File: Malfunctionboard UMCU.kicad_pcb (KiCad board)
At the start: 2 copper layers, 144.9 x 32.7 mm, 265 parts, among them J101 Conn_02x05_Odd_Even, J102 Conn_02x05_Odd_Even, J201 Conn_Coaxial, J202 Conn_Coaxial, J301 Conn_Coaxial, J302 Conn_Coaxial, J401 Conn_Coaxial, J402 Conn_Coaxial, J501 Conn_Coaxial, J502 Conn_Coaxial, J601 Conn_Coaxial, J602 Conn_Coaxial, J701 Conn_Coaxial, J702 Conn_Coaxial, J801 Conn_Coaxial, J802 Conn_Coaxial, J901 Conn_Coaxial, J902 Conn_Coaxial, Q101 NTR5103NT1G, Q102 RSC002P03T316, Q103 RSC002P03T316, Q104 NTR5103NT1G, Q201 NTR5103NT1G, Q202 NTR5103NT1G, Q301 NTR5103NT1G, Q302 NTR5103NT1G, Q401 NTR5103NT1G, Q402 NTR5103NT1G, Q501 NTR5103NT1G, Q502 NTR5103NT1G, Q601 NTR5103NT1G, Q602 NTR5103NT1G, Q701 NTR5103NT1G, Q702 NTR5103NT1G, Q801 NTR5103NT1G, Q802 NTR5103NT1G, Q901 NTR5103NT1G, Q902 NTR5103NT1G, U201 LM339PW, U301 LM339PW, U401 LM339PW, U501 LM339PW, U601 LM339PW, U701 LM339PW, U801 LM339PW, U901 LM339PW

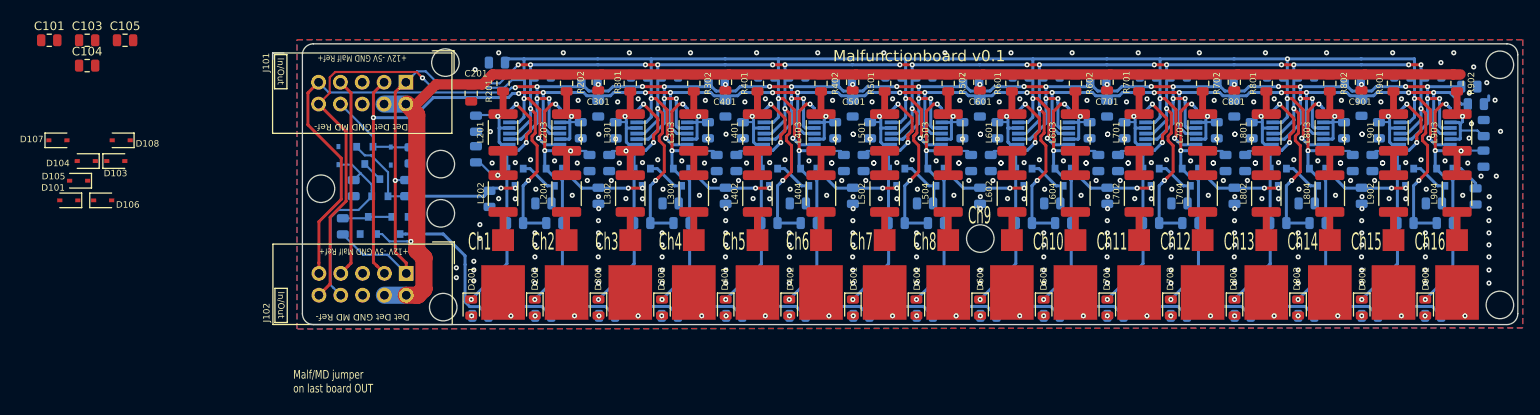
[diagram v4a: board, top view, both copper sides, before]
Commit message: changed: Added extra protection C's to v0.1
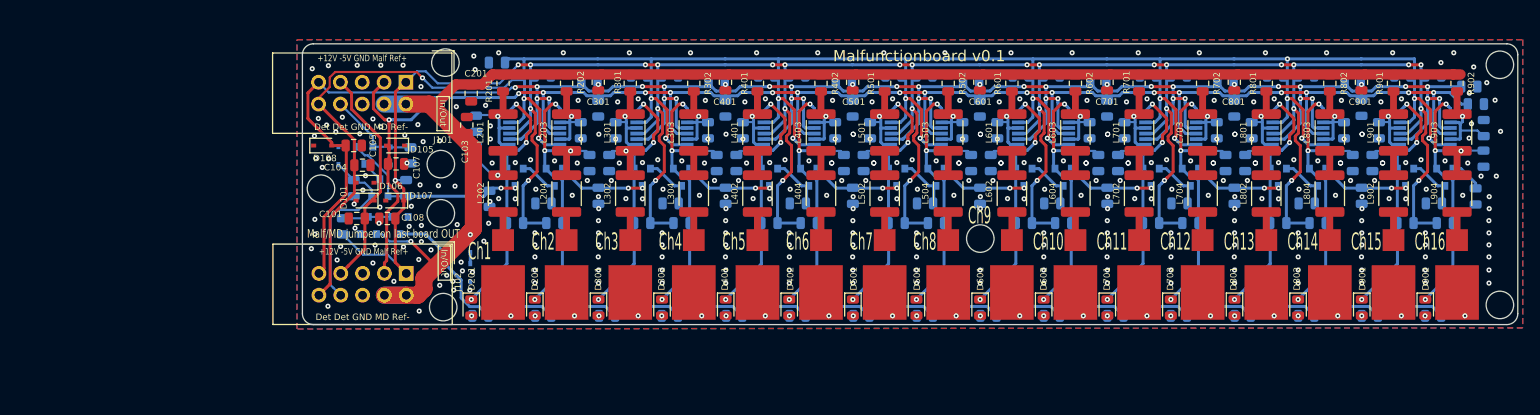
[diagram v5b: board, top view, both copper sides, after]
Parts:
- added C107: 10n, Capacitor_SMD:C_0805_2012Metric, F.Cu at (80.1, 114.9)
- added C108: 10n, Capacitor_SMD:C_0805_2012Metric, F.Cu at (79.1, 121.3)
- D103, D104: moved to B.Cu
- moved D104 46.5 mm to (88.7, 127.6), turned to 270 degrees
- moved C103 45.3 mm to (88.3, 110.4), turned to 270 degrees
- moved D103 42.4 mm to (88.7, 124.2), turned to 90 degrees
- moved C101 41.4 mm to (75.5, 121.3)
- moved D107 39.8 mm to (80.0, 119.2), turned to 180 degrees
- moved D105 37.1 mm to (80.1, 112.8)
- moved D101 34.5 mm to (76.5, 119.2)
- moved C104 34.1 mm to (76.2, 115.1), turned to 180 degrees
- moved D106 30.6 mm to (76.5, 117.1), turned to 180 degrees
- moved C105 29.3 mm to (75.2, 112.8), turned to 180 degrees
- moved D108 23.5 mm to (71.6, 112.8), turned to 0 degrees
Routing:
- net /V_in: track 157.7 -> 170.7 mm, vias 1 -> 2
- net /Malf: track 23.2 -> 26.5 mm
- net Net-(C106-Pad2): track 22.7 -> 21.2 mm
- net /Ref+: track 276.5 -> 277.8 mm
- net Net-(D103-Pad1): track 0.00 -> 1.29 mm
- net /sheet5DD8DCB3/LED_GND: track 142.3 -> 141.1 mm
- net /Ref-: track 301.0 -> 302.1 mm
- net -5V: track 209.5 -> 210.5 mm
- net +12V: track 374.8 -> 375.6 mm
- net GND: vias 301 -> 358
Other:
- board size 144.9 x 32.7 mm -> 141.4 x 32.7 mm

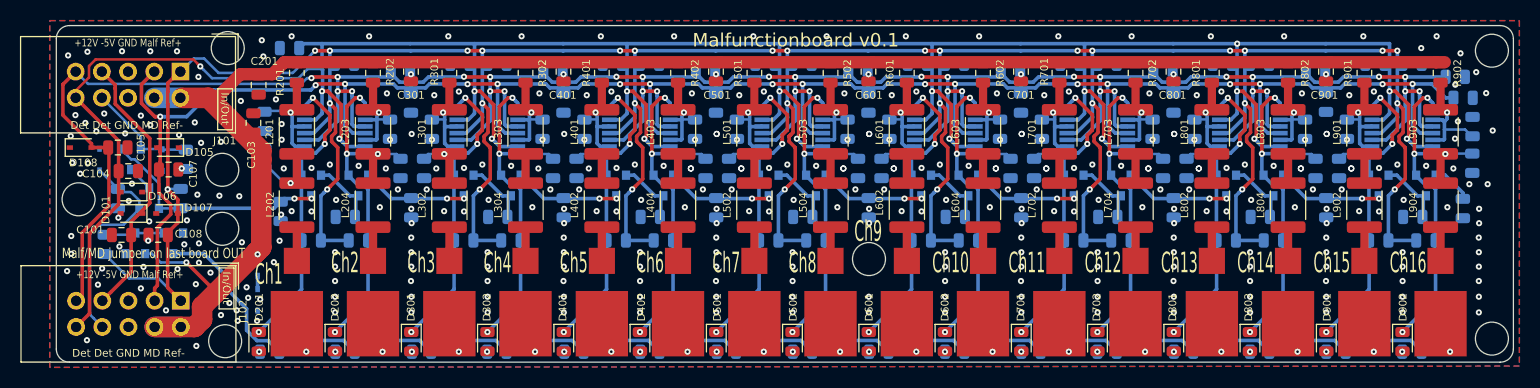
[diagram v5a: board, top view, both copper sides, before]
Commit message: Ready for ordering. Changed: some overlapping via's, moved mounting holes slightly and made them plated.
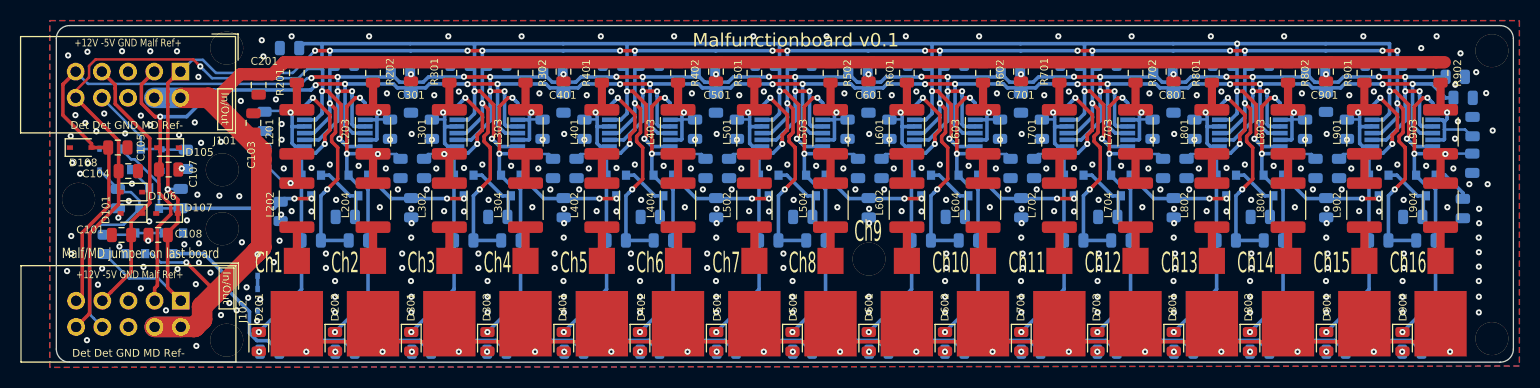
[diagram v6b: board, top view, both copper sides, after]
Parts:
- H101 (x2), H102, H104, H105, H106, H107, H108: footprint MountingHole:MountingHole_3.2mm_M3 -> _Custom:MountingHole_3.2mm_M3_plated
- moved H108 0.18 mm to (85.8, 131.5)
- moved H107 0.10 mm to (85.8, 103.1)
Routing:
- net GND: track 0.00 -> 112.4 mm, vias 358 -> 342
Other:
- board text added: "Malf/MD jumper on last board"
- board text removed: "Malf/MD jumper on last board OUT"

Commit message: Changed: small changes
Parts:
- added R104: R_Ref-, Resistor_SMD:R_0805_2012Metric, B.Cu at (84.8, 109.5)
- added R105: R_Ref, Resistor_SMD:R_0805_2012Metric, B.Cu at (84.8, 107.4)
- added R106: R_Ref+, Resistor_SMD:R_0805_2012Metric, B.Cu at (87.6, 108.2)
- moved C202 0.51 mm to (89.9, 110.2)
- moved C203 0.25 mm to (89.7, 113.8)
- moved C102 0.13 mm to (81.7, 113.9)
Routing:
- net /Ref+: track 277.8 -> 284.1 mm
- net -5V: track 210.5 -> 214.6 mm
- net /Ref-: track 302.1 -> 305.4 mm
- net GND: vias 342 -> 339
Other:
- board text added: "(If no ext ref) Optional"
